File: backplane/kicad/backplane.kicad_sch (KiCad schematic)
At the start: 14 parts, among them J1 Conn_01x02_Pin

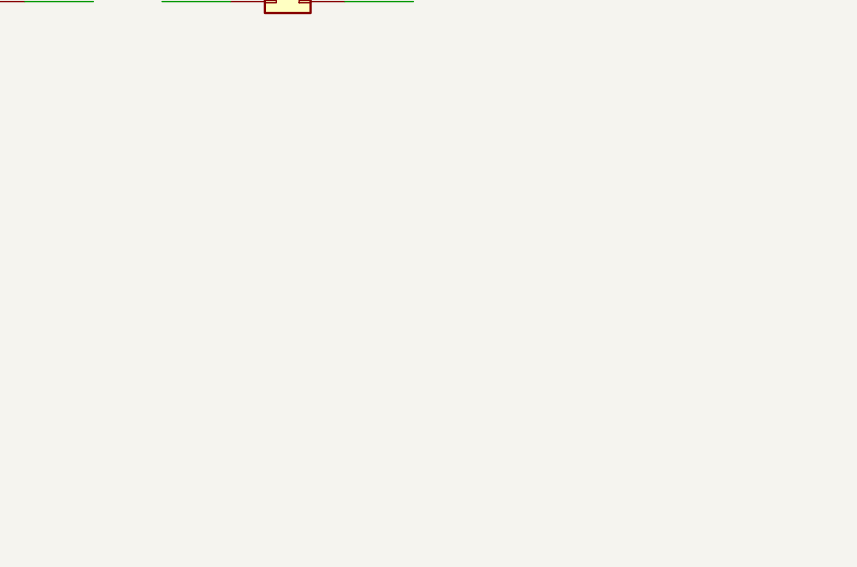
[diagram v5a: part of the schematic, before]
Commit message: Added comments to the Backplane schematic.
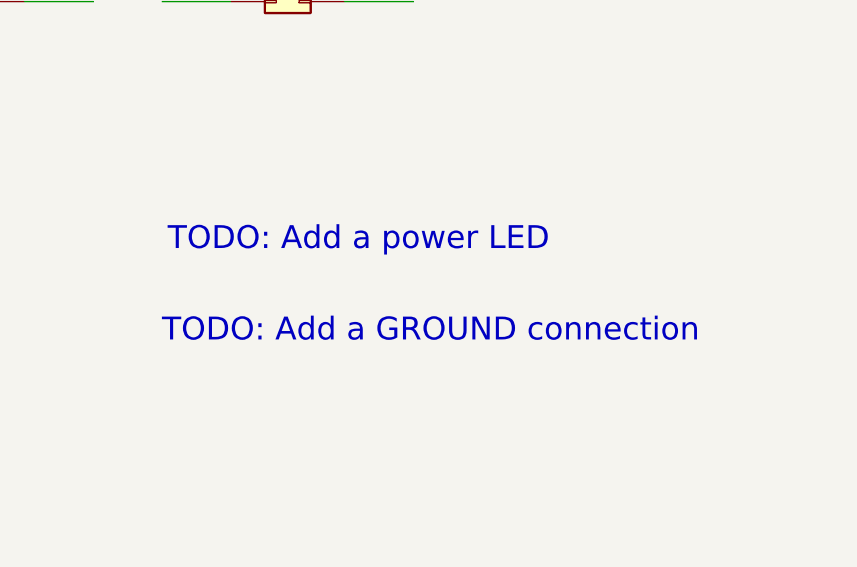
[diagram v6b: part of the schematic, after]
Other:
- note added: "TODO: Add a GROUND connection"
- note added: "TODO: Add a power LED"
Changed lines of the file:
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@@
     (stroke (width 0) (type default))
+  )
+  (text "TODO: Add a power LED" (at 264.795 213.36 0)
+    (effects (font (size 2.54 2.54) (color 255 0 0 1)) (justify left bottom))
+  )
+  (text "TODO: Add a GROUND connection" (at 264.16 223.52 0)
+    (effects (font (size 2.54 2.54) (color 255 0 0 1)) (justify left bottom))
   )
   (label "A29" (at 149.86 134.62 180) (fields_autoplaced)

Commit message: Cleaned up TODOs for next version of backplane.
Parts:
- added TP1, TP2, TP3, TP4: TestPoint, common:Test_Pad, symbol Connector:TestPoint
- H1, H2, H3, H4, H5, H6: symbol Mechanical:MountingHole -> Mechanical:MountingHole_Pad
- J1: footprint backplane:JST_XH_B2B-XH-AM_1x02_P2.50mm_Vertical -> backplane:TerminalBlock_3P_7.62mm; symbol Connector_Generic:Conn_01x02 -> Connector_Generic:Conn_01x03; LCSC (none) -> C557662
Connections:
- net +5V: now also TP4.1
- net GND: now also J1.1 (Pin_1), TP3.1
- net VIN+: now also J1.3 (Pin_3), TP1.1; no longer J1.2 (Pin_2)
- net VIN-: now also J1.2 (Pin_2), TP2.1; no longer J1.1 (Pin_1)
- no-connect marks 0 -> 6
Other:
- note removed: "TODO: Add a GROUND connection"
- note removed: "TODO: Add a power LED"

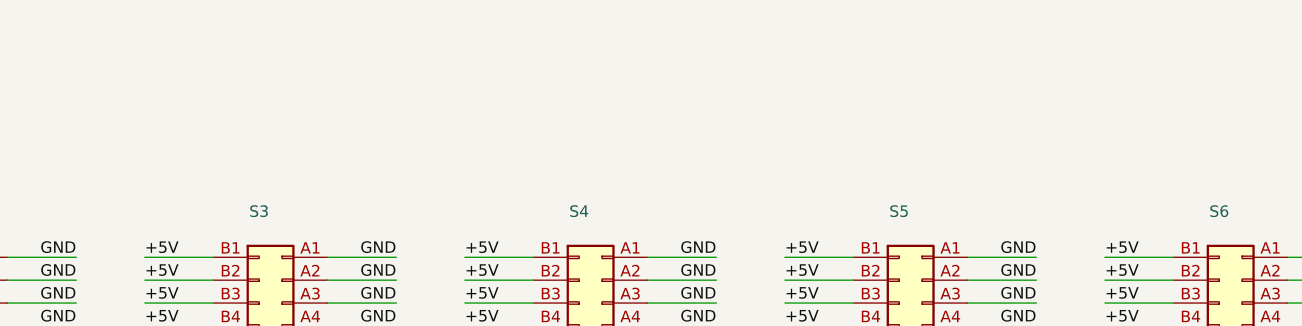
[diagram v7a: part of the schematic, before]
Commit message: Added TODOs to kicad schematics (adding a serial number silkscreen)
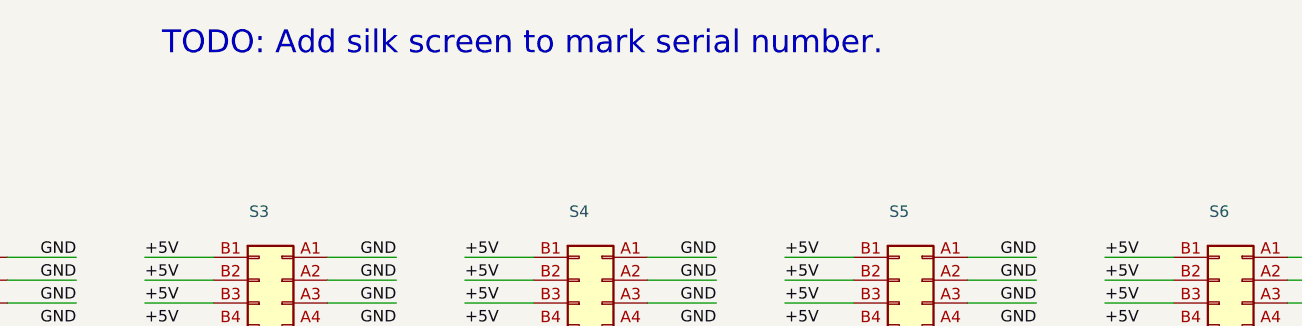
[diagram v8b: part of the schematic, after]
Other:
- note added: "TODO: Add silk screen to mark serial number."
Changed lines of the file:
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@@
     (stroke (width 0) (type default))
+  )
+  (text "TODO: Add silk screen to mark serial number." (at 123.825 36.195 0)
+    (effects (font (size 2.54 2.54) (color 255 0 0 1)) (justify left bottom))
   )
   (label "A29" (at 149.86 134.62 180) (fields_autoplaced)
